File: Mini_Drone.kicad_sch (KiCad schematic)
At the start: 0 parts

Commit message: Motor Drivers no cap
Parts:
- added D1, D2, D3, D4: SS24, Diode_SMD:D_SMA, symbol Diode:SS24
- added Q1, Q2, Q3, Q4: AO3400A, Package_TO_SOT_SMD:SOT-23, symbol Transistor_FET:AO3400A
- added R1, R2, R3, R4: R, symbol Device:R
- added TP1, TP10, TP11, TP12, TP2, TP3, TP4, TP5, TP6, TP7, TP8, TP9: TestPoint, symbol Connector:TestPoint
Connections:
- new net: D4.2 (A), Q4.3 (D), TP12.1
- new net: D1.1 (K), TP1.1, TP2.1
- new net: D3.2 (A), Q3.3 (D), TP11.1
- new net: D2.1 (K), TP3.1, TP4.1
- new net: D2.2 (A), Q2.3 (D), TP10.1
- new net: D4.1 (K), TP7.1, TP8.1
- new net: D3.1 (K), TP5.1, TP6.1
- new net: D1.2 (A), Q1.3 (D), TP9.1
- new net GND: Q1.2 (S), Q2.2 (S), Q3.2 (S), Q4.2 (S), R1.2, R2.2, R3.2, R4.2
- new net GPIO: Q1.1 (G), Q2.1 (G), Q3.1 (G), Q4.1 (G), R1.1, R2.1, R3.1, R4.1

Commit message: Version 1
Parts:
- removed D1, D2, D3, D4: SS24, Diode_SMD:D_SMA, symbol Diode:SS24
- removed TP1, TP3, TP5, TP7: TestPoint, symbol Connector:TestPoint
- added C1, C4: 10nf, Capacitor_SMD:C_0201_0603Metric_Pad0.64x0.40mm_HandSolder, symbol Device:C
- added C2: 100nf, Capacitor_SMD:C_0201_0603Metric_Pad0.64x0.40mm_HandSolder, symbol Device:C
- added C3: 1uf, Capacitor_SMD:C_0201_0603Metric_Pad0.64x0.40mm_HandSolder, symbol Device:C
- added D1, D3, D4, D5: 1N4148W, Diode_SMD:D_SOD-123, symbol Diode:1N4148W
- added J1: Conn_01x02, Connector_JST:JST_EH_S2B-EH_1x02_P2.50mm_Horizontal, symbol Connector_Generic:Conn_01x02
- added R5, R6, R7: R, Resistor_SMD:R_0201_0603Metric_Pad0.64x0.40mm_HandSolder, symbol Device:R
- added U1: XIAO ESP32-S3, Drone_prj:XIAO ESP32-S3, symbol Drone_prj:XIAO ESP32-S3
- added U2: MPU-6050, Sensor_Motion:InvenSense_QFN-24_4x4mm_P0.5mm, symbol Sensor_Motion:MPU-6050
- R1, R2, R3, R4: footprint (none) -> Resistor_SMD:R_0201_0603Metric_Pad0.64x0.40mm_HandSolder
- TP1: renamed from TP2; footprint (none) -> TestPoint:TestPoint_Pad_1.5x1.5mm
- TP2: renamed from TP4; footprint (none) -> TestPoint:TestPoint_Pad_1.5x1.5mm
- TP3: renamed from TP6; footprint (none) -> TestPoint:TestPoint_Pad_1.5x1.5mm
- TP4: renamed from TP8; footprint (none) -> TestPoint:TestPoint_Pad_1.5x1.5mm
- TP5: renamed from TP9; footprint (none) -> TestPoint:TestPoint_Pad_1.5x1.5mm
- TP6: renamed from TP10; footprint (none) -> TestPoint:TestPoint_Pad_1.5x1.5mm
- TP7: renamed from TP11; footprint (none) -> TestPoint:TestPoint_Pad_1.5x1.5mm
- TP8: renamed from TP12; footprint (none) -> TestPoint:TestPoint_Pad_1.5x1.5mm
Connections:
- net GND: now also C1.2, C2.2, C3.2, C4.2, J1.2 (Pin_2), U1.13 (GND), U2.1 (CLKIN), U2.11 (FSYNC), U2.18 (GND), U2.9 (AD0)
- net at Q4.3 (D), TP8.1: now also D3.2 (A)
- net BAT+: now reaches TP1.1
- net BAT+: now also TP2.1, TP3.1, TP4.1, D1.1 (K), D3.1 (K), D4.1 (K), D5.1 (K), J1.1 (Pin_1)
- net at Q3.3 (D), TP7.1: now also D1.2 (A)
- net at Q2.3 (D), TP6.1: now also D5.2 (A)
- net at Q1.3 (D), TP5.1: now also D4.2 (A)
- removed net GPIO: Q1.1 (G), Q2.1 (G), Q3.1 (G), Q4.1 (G), R1.1, R2.1, R3.1, R4.1
- new net: C3.1, U2.10 (REGOUT)
- new net: R7.2, U2.12 (INT)
- new net: C4.1, U2.20 (CPOUT)
- new net +3V3: C1.1, C2.1, R5.1, R6.1, R7.1, U1.12 (VCC_3V3), U2.13 (VDD), U2.8 (VLOGIC)
- new net D0: Q1.1 (G), R1.1, U1.1 (D0)
- new net D1: Q2.1 (G), R2.1, U1.2 (D1)
- new net D2: Q3.1 (G), R3.1, U1.3 (D2)
- new net D3: Q4.1 (G), R4.1, U1.4 (D3)
- new net SCL: R5.2, U1.6 (D5), U2.23 (SCL)
- new net SDA: R6.2, U1.5 (D4), U2.24 (SDA)
- no-connect marks 0 -> 8

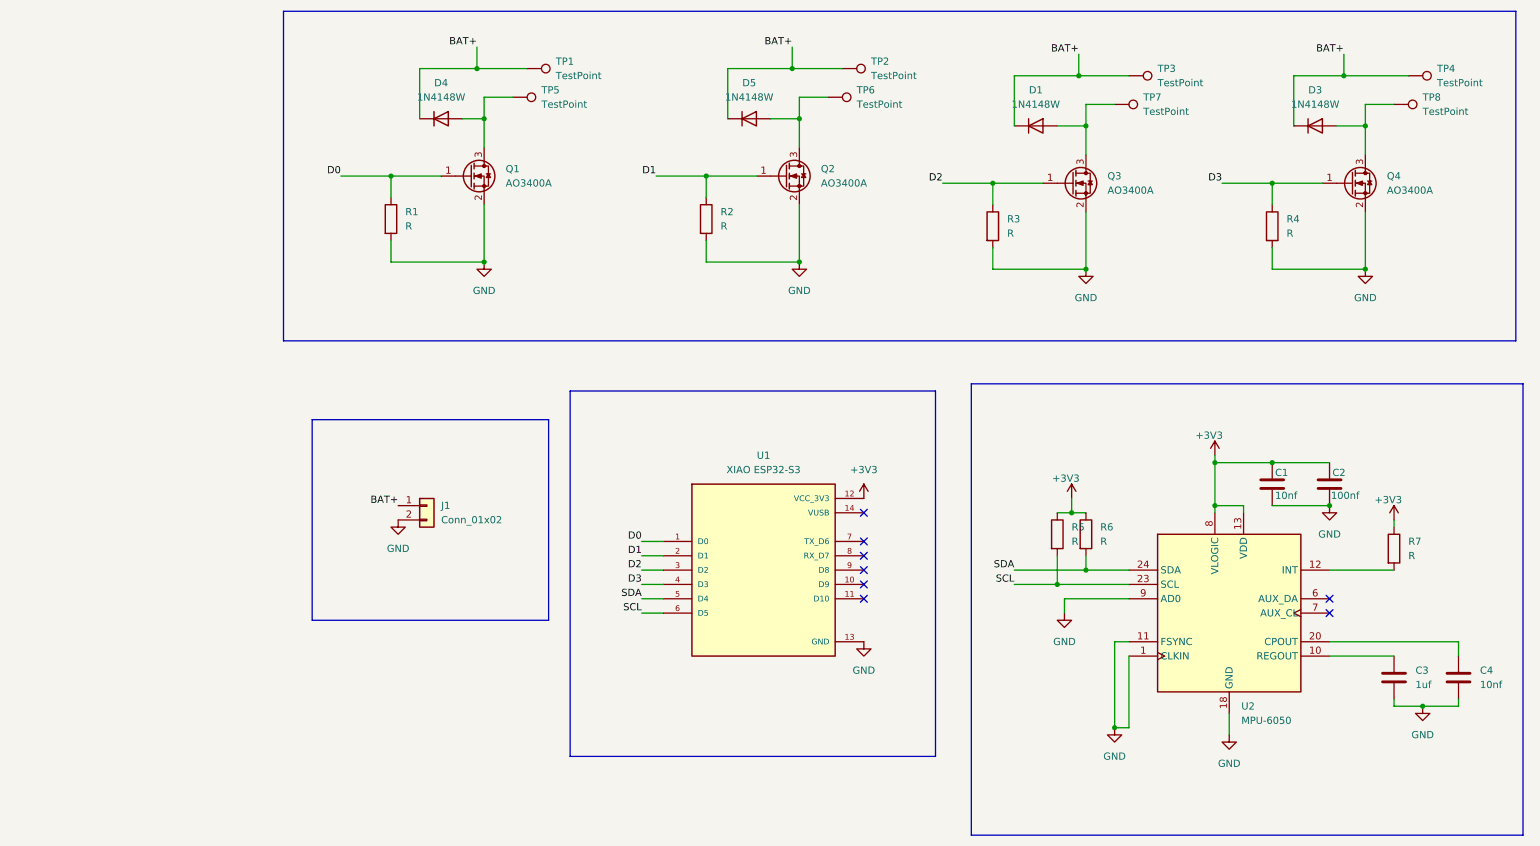
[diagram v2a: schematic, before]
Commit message: drc for sch checked
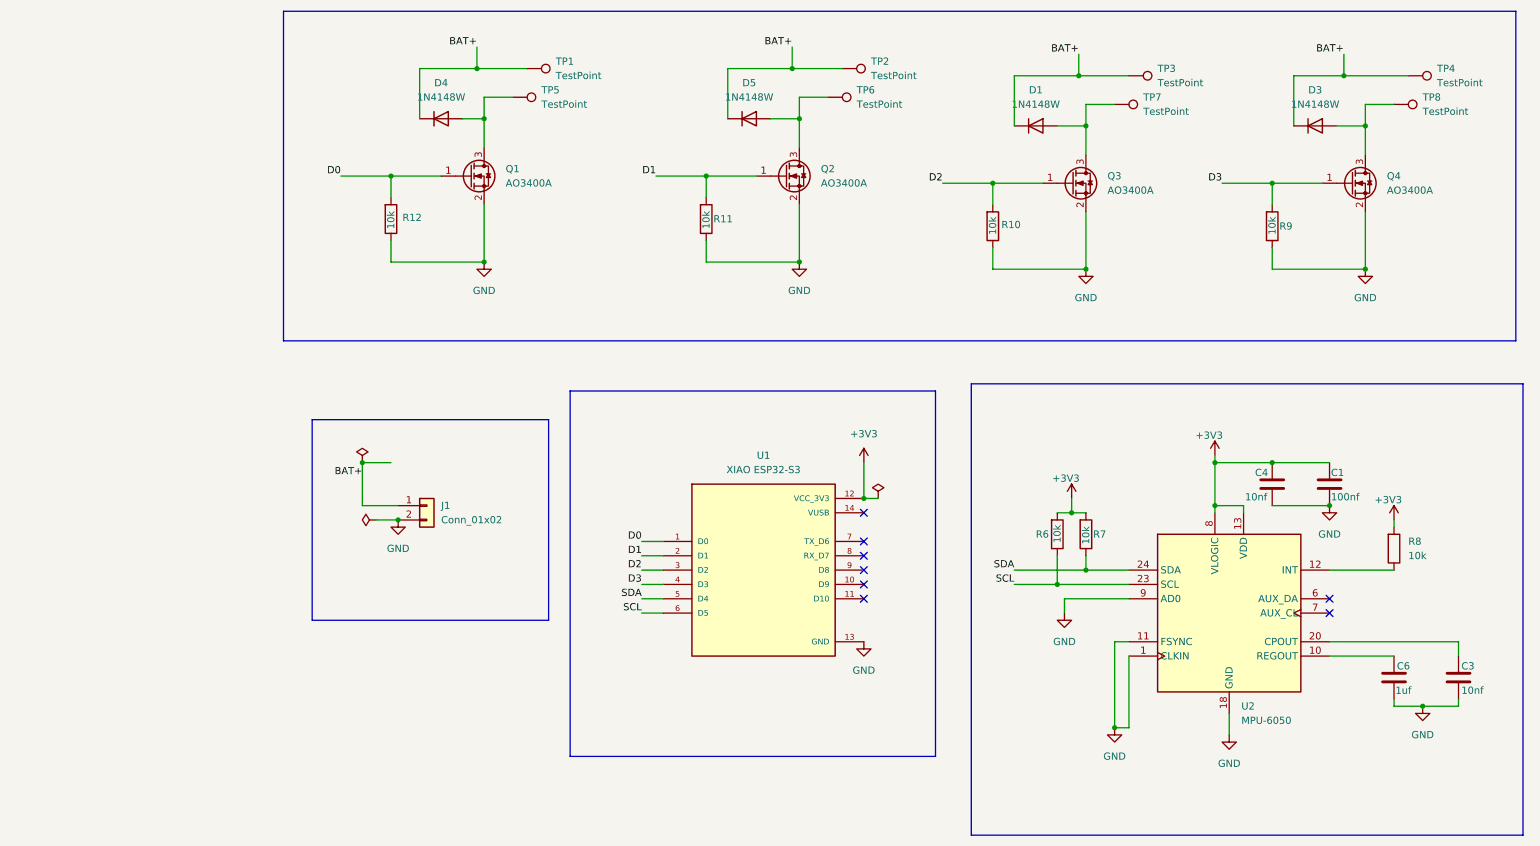
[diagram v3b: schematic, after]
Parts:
- removed C1, C4: 10nf, Capacitor_SMD:C_0201_0603Metric_Pad0.64x0.40mm_HandSolder, symbol Device:C
- removed C2: 100nf, Capacitor_SMD:C_0201_0603Metric_Pad0.64x0.40mm_HandSolder, symbol Device:C
- removed C3: 1uf, Capacitor_SMD:C_0201_0603Metric_Pad0.64x0.40mm_HandSolder, symbol Device:C
- removed R1, R2, R3, R4, R5, R6, R7: R, Resistor_SMD:R_0201_0603Metric_Pad0.64x0.40mm_HandSolder, symbol Device:R
- added C1: 100nf, symbol Drone_prj:C_100nf
- added C3, C4: 10nf, symbol Drone_prj:c_10nf
- added C6: 1uf, symbol Drone_prj:C_1uf
- added R10, R11, R12, R6, R7, R8, R9: 10k, Resistor_SMD:R_0603_1608Metric, symbol Drone_prj:Resistor_SMD{colon}R_0603_1608Metric
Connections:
- net +3V3: now also C1.1, C4.1, R6.1, R7.1, R8.1
- net D0: now also R12.1
- net D1: now also R11.1
- net D2: now also R10.1
- net D3: now also R9.1
- net GND: now also C1.2, C3.2, C4.2, C6.2, R10.2, R11.2, R12.2, R9.2
- net SCL: now also R6.2
- net SDA: now also R7.2
- net at U2.10 (REGOUT): now also C6.1
- net at U2.12 (INT): now also R8.2
- net at U2.20 (CPOUT): now also C3.1

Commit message: 1 unconnected
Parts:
- removed D1, D3, D4, D5: 1N4148W, Diode_SMD:D_SOD-123, symbol Diode:1N4148W
- added C5, C6, C7, C8: 1uf, Capacitor_SMD:C_0603_1608Metric, symbol Drone_prj:C_1uf
- added D1, D2, D3, D5: 1N4148WT, Diode_SMD:D_SOD-523, symbol Diode:1N4148WT
- added R8, R9: 10k, Resistor_SMD:R_0603_1608Metric, symbol Drone_prj:Resistor_SMD{colon}R_0603_1608Metric
- added TP10, TP9: TestPoint, TestPoint:TestPoint_Pad_1.5x1.5mm, symbol Connector:TestPoint
- C1: renamed from C4; footprint (none) -> Capacitor_SMD:C_0603_1608Metric
- C2: renamed from C1; footprint (none) -> Capacitor_SMD:C_0603_1608Metric
- C3: renamed from C6; footprint (none) -> Capacitor_SMD:C_0603_1608Metric
- C4: renamed from C3; footprint (none) -> Capacitor_SMD:C_0603_1608Metric
- TP1, TP2, TP3, TP4, TP5, TP6, TP7, TP8: footprint TestPoint:TestPoint_Pad_1.5x1.5mm -> TestPoint:TestPoint_Pad_D1.0mm
- renumbered R12 to R1, R11 to R2, R10 to R3, R9 to R4, R6 to R5, R7 to R6, R8 to R7
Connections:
- net BAT+: now also C5.1, C6.1, C7.1, C8.1, D1.1 (K), D2.1 (K), D3.1 (K), D5.1 (K), R8.1, TP9.1
- net D1: no longer Q2.1 (G), R2.1
- net D2: now also R8.2, R9.1; no longer Q3.1 (G), R3.1
- net D3: now also Q3.1 (G), R3.1; no longer Q4.1 (G), R4.1
- net GND: now also R9.2, TP10.1
- net at Q4.3 (D), TP8.1: now also C8.2, D3.2 (A)
- net D10: now reaches U1.11 (D10)
- net D10: now also Q2.1 (G), R2.1
- net D8: now reaches U1.9 (D8)
- net D8: now also Q4.1 (G), R4.1
- net at Q3.3 (D), TP7.1: now also C7.2, D2.2 (A)
- net at Q2.3 (D), TP6.1: now also C6.2, D1.2 (A)
- net at Q1.3 (D), TP5.1: now also C5.2, D5.2 (A)
- no-connect marks 8 -> 6
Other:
- moved on the sheet: J1, TP1, U1

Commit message: good progress
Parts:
- U2: footprint Sensor_Motion:InvenSense_QFN-24_4x4mm_P0.5mm -> Drone_prj:InvenSense_QFN-24_4x4mm_P0.5mm
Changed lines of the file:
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@@
+		(length 2.54)
+		(shape round)
+		(at 195.58 116.84 180)
+		(fields_autoplaced yes)
+		(effects
+			(font
+				(size 1.27 1.27)
+			)
+			(justify right bottom)
+		)
+		(property "Netclass" "i2c_lines"
+			(at 196.2785 119.38 0)
+			(effects
+				(font
+					(size 1.27 1.27)
+				)
+				(justify left)
+			)
+		)
+		(property "Component Class" ""
+			(at -88.9 2.54 0)
+			(effects
+				(font
+					(size 1.27 1.27)
+					(italic yes)
+				)
+			)
+		)
+	)
+	(netclass_flag ""
 		(length 2.54)
 		(shape round)
@@
 		(property "Component Class" ""
 			(at -69.85 -11.43 0)
+			(effects
+				(font
+					(size 1.27 1.27)
+					(italic yes)
+				)
+			)
+		)
+	)
+	(netclass_flag ""
+		(length 2.54)
+		(shape round)
+		(at 193.04 114.3 0)
+		(fields_autoplaced yes)
+		(effects
+			(font
+				(size 1.27 1.27)
+			)
+			(justify left bottom)
+		)
+		(property "Netclass" "i2c_lines"
+			(at 193.7385 111.76 0)
+			(effects
+				(font
+					(size 1.27 1.27)
+				)
+				(justify left)
+			)
+		)
+		(property "Component Class" ""
+			(at -91.44 0 0)
 			(effects
 				(font
@@
 			)
 		)
-		(property "Footprint" "Sensor_Motion:InvenSense_QFN-24_4x4mm_P0.5mm"
+		(property "Footprint" "Drone_prj:InvenSense_QFN-24_4x4mm_P0.5mm"
 			(at 231.14 142.24 0)
 			(effects

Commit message: sch organized no error success
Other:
- note added: "BATTERY CONNECTOR"
- note added: "IMU"
- note added: "MOTOR DRIVER"
- note added: "SOS"
- moved on the sheet: C1, C2, C3, C4, C5, C6, C7, C8, D1, D2, D3, D5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
